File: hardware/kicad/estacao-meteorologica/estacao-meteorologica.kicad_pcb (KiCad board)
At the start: 2 copper layers, 124.6 x 76.8 mm, 127 parts, among them J101 Header, 1x02, P2.54 mm, J102 Header, 1x06, P2.54 mm, J103 Header, 1x03, P2.54 mm, J301 RJ11 6P6C, 90°, J401 RJ11 6P6C, 90°, J501 RJ11 6P6C, 90°, J601 DC jack, 2.0 mm, J602 JST-XH, 1x02, P2.50 mm, J701 U.FL, 50 Ω, J801 microSD socket, TF-15x15, Q601 DMP6023LE-13, SW101 Tactile switch, SPST, U101 STM32F446RET6, U211 BMP280, U221 BH1750FVI-TR, U231 DHT22, U301 SN74LVC1G17DBVR, U401 SN74LVC1G17DBVR, U601 AP63205WU-7, U602 TLV62569DBVR, U701 LORA1276-C1-915MHZ, U801 SN74LVC125APWR, U802 EMIF06-MSD02N16, Y101 32.768 kHz, CL 7 pF, Y102 8 MHz, CL 10 pF

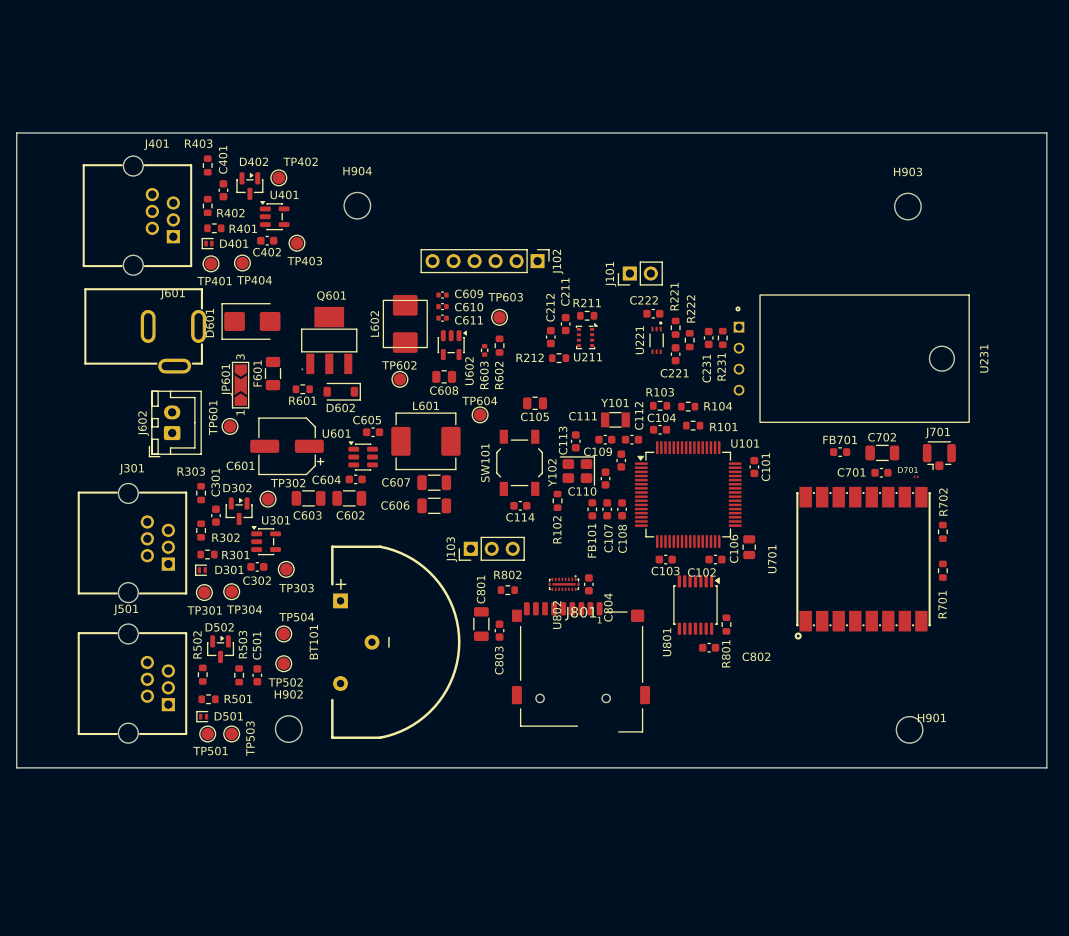
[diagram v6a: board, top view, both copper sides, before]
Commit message: Roteamento 2.0 - rj11 compartilhado biruta e anemometro
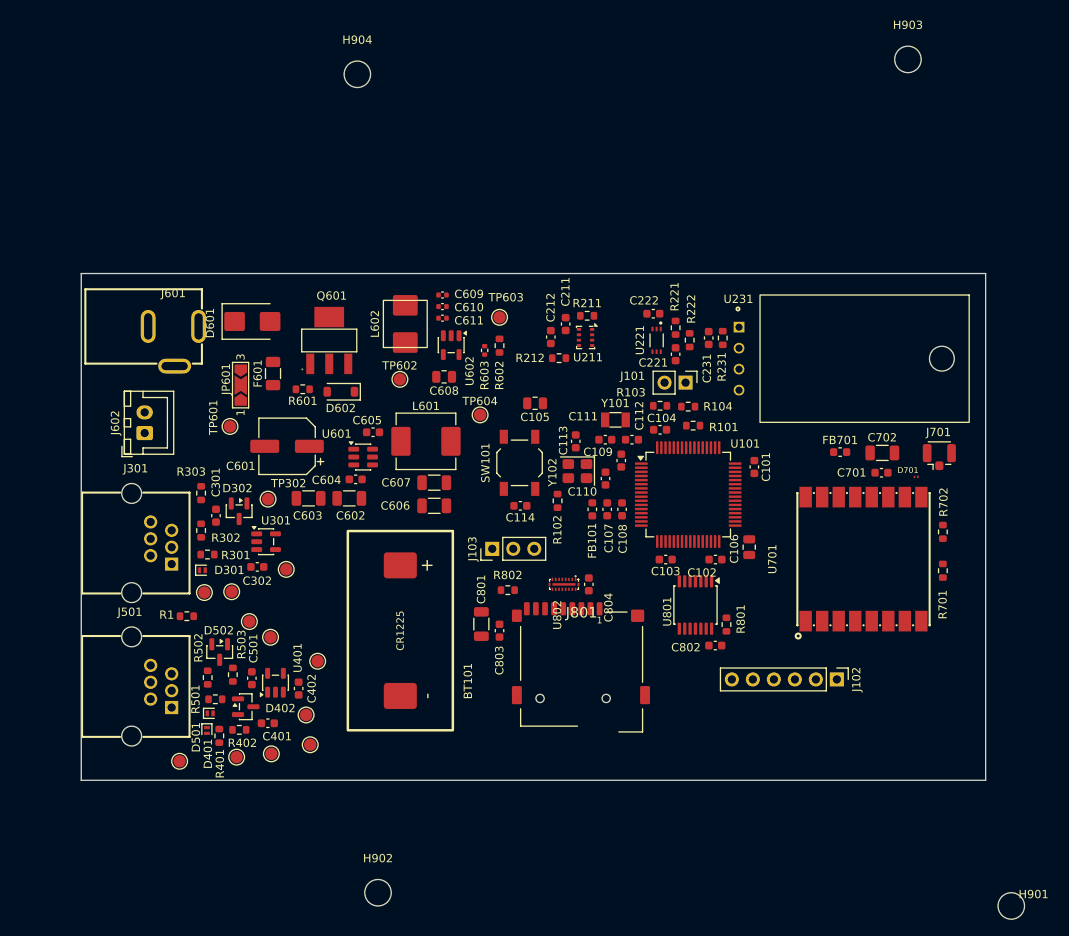
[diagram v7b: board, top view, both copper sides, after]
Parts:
- removed J401: RJ11 6P6C, 90°, Sensores_Meteo:RJ11-TH_PCB-6P6C-90
- removed R403: 1 kΩ, Resistor_SMD:R_0603_1608Metric
- added R1: 1 kΩ, Resistor_SMD:R_0603_1608Metric, F.Cu at (51.2, 93.5)
- BT101: value CR2032 holder, vertical -> CR1225 holder, horizontal; footprint Hardware_MCU:BT_Holder_MPD_BS-5_Vertical -> Hardware_Battery:BT_Holder_MYOUNG_BS-12-B4AK025-R
- moved TP402 65.1 mm to (65.6, 105.4)
- moved C401 64.7 mm to (61.0, 106.4), turned to 0 degrees
- moved R402 63.5 mm to (57.5, 107.2), turned to 0 degrees
- moved D402 63.0 mm to (58.3, 104.4), turned to 0 degrees
- moved J102 62.2 mm to (129.8, 101.1)
- moved R401 61.4 mm to (55.1, 107.9), turned to 90 degrees
- moved TP401 59.8 mm to (57.2, 110.5)
- moved D401 58.9 mm to (53.6, 107.3), turned to -90 degrees
- moved TP404 58.8 mm to (66.1, 109.0)
- moved U401 56.4 mm to (61.9, 101.5), turned to 90 degrees
- moved C402 54.3 mm to (64.7, 102.2), turned to -90 degrees
- moved TP403 50.6 mm to (67.0, 98.9)
- moved H901 24.6 mm to (150.9, 128.5)
- moved H902 22.6 mm to (74.3, 126.9)
- moved H903 17.8 mm to (138.4, 26.1)
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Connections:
- D401 pad 1: /INTERFACES METEOROLÓGICAS/ANEMÔMETRO/SENS_WIND_SPEED_RAW -> SENS_WIND_SPEED_RAW
- J501 pad 3: +3V3 -> Net-(J501-Pad3)
- J501 pad 4: unconnected-(J501-Pad4) -> SENS_WIND_SPEED_RAW
- R401 pad 2: /INTERFACES METEOROLÓGICAS/ANEMÔMETRO/SENS_WIND_SPEED_RAW -> SENS_WIND_SPEED_RAW
- R402 pad 1: /INTERFACES METEOROLÓGICAS/ANEMÔMETRO/SENS_WIND_SPEED_RAW -> SENS_WIND_SPEED_RAW
- TP401 pad 1: /INTERFACES METEOROLÓGICAS/ANEMÔMETRO/SENS_WIND_SPEED_RAW -> SENS_WIND_SPEED_RAW
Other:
- board size 124.6 x 76.8 mm -> 109.4 x 61.3 mm

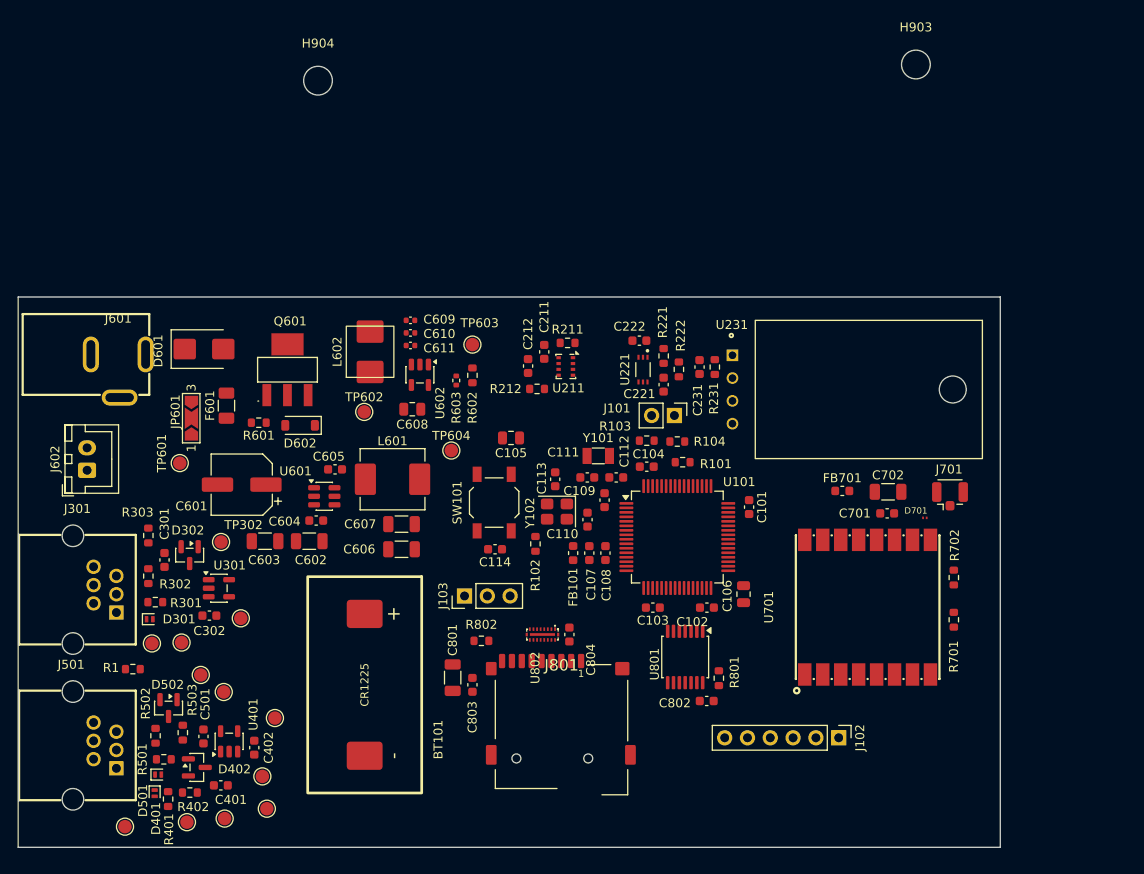
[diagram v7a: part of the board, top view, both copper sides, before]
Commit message: Refact - mudança do sensor bh1750 para placa filha e conector jst + reposicionamento do sensor DHT22 para reduzir influencia de temperatura interna da placa
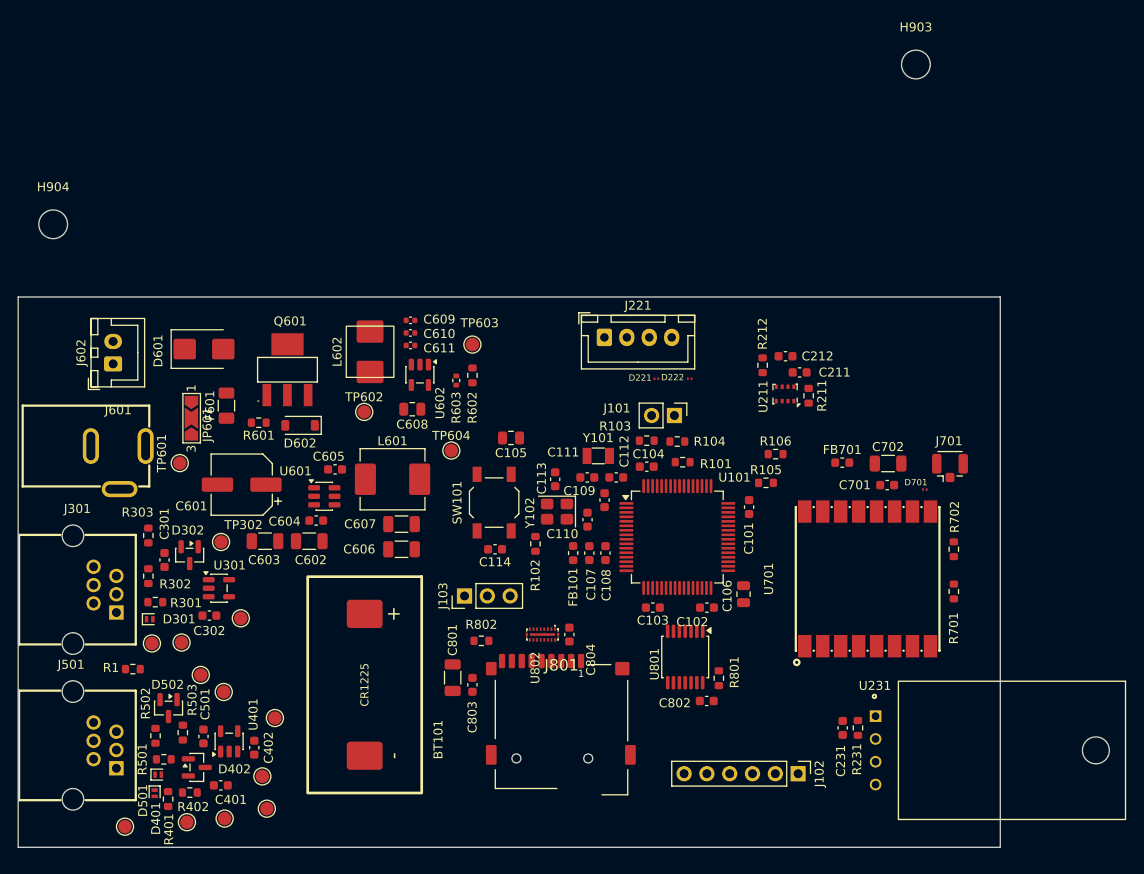
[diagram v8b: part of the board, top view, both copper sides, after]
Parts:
- removed C221: 1 µF, Capacitor_SMD:C_0603_1608Metric
- removed C222: 100 nF, Capacitor_SMD:C_0603_1608Metric
- removed R221: 10 kΩ, Resistor_SMD:R_0603_1608Metric
- removed R222: 1 kΩ, Resistor_SMD:R_0603_1608Metric
- removed U221: BH1750FVI-TR, Hardware_Sensors:BH1750FVI-TR_WSOF-6
- added D221: PESD5V0R1BSFYL, Hardware_LoRa:SOD-962_L0.6-W0.3-BI, F.Cu at (109.5, 61.1)
- added D222: PESD5V0R1BSFYL, Hardware_LoRa:SOD-962_L0.6-W0.3-BI, F.Cu at (113.2, 61.1)
- added J221: JST-XH, 1x04, P2.50 mm, Connector_JST:JST_XH_B4B-XH-A_1x04_P2.50mm_Vertical, F.Cu at (103.7, 56.5)
- added R105: 4.7k, Resistor_SMD:R_0603_1608Metric, F.Cu at (121.7, 72.7)
- added R106: 4.7k, Resistor_SMD:R_0603_1608Metric, F.Cu at (122.8, 69.5)
- moved C231 43.2 mm to (130.2, 100.0)
- moved R231 43.2 mm to (131.9, 100.0)
- moved U231 43.2 mm to (149.1, 102.5)
- moved H904 33.6 mm to (42.3, 43.9)
- moved C212 28.7 mm to (123.9, 58.6), turned to 0 degrees
- moved C211 28.5 mm to (125.5, 60.4), turned to 180 degrees
- moved R211 27.5 mm to (126.5, 63.0), turned to -90 degrees
- moved R212 25.3 mm to (121.3, 59.6), turned to -90 degrees
- moved U211 24.6 mm to (123.8, 62.8), turned to 180 degrees
- moved J602 12.2 mm to (49.0, 59.5)
- moved J601 10.2 mm to (49.5, 71.0)
- moved J102 6.04 mm to (125.3, 105.1)
- moved C702 3.15 mm to (135.3, 70.5)
- moved J701 3.15 mm to (142.2, 71.0)
- moved R701 3.15 mm to (142.6, 84.8)
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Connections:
- U101 pad 40: unconnected-(U101-PC9-Pad40) -> BH_I2C3_SDA
- U101 pad 41: /MCU E DEPURAÇÃO/DHT22_DATA -> BH_I2C3_SCL
- U101 pad 42: unconnected-(U101-PA9-Pad42) -> /MCU E DEPURAÇÃO/DHT22_DATA
